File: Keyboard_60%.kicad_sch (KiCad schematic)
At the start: 51 parts, among them J3 Prog_conn, J5 Tag connect TC2030-CTX, SW2 Reset Switch, U3 nRF52840-QIAA-R/nRF52833-QIAA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, Y1 32MHz, Y2 32.768kHz

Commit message: Finalized hardware Ver 1 release
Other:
- company: (none) -> HW-tinkerers
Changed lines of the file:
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@@
   (title_block
     (title "Main Page")
-    (date "2023-06-05")
+    (date "2024-02-17")
     (rev "1.0")
+    (company "HW-tinkerers")
   )
   (junction (at 96.52 181.61) (diameter 0) (color 0 0 0 0)

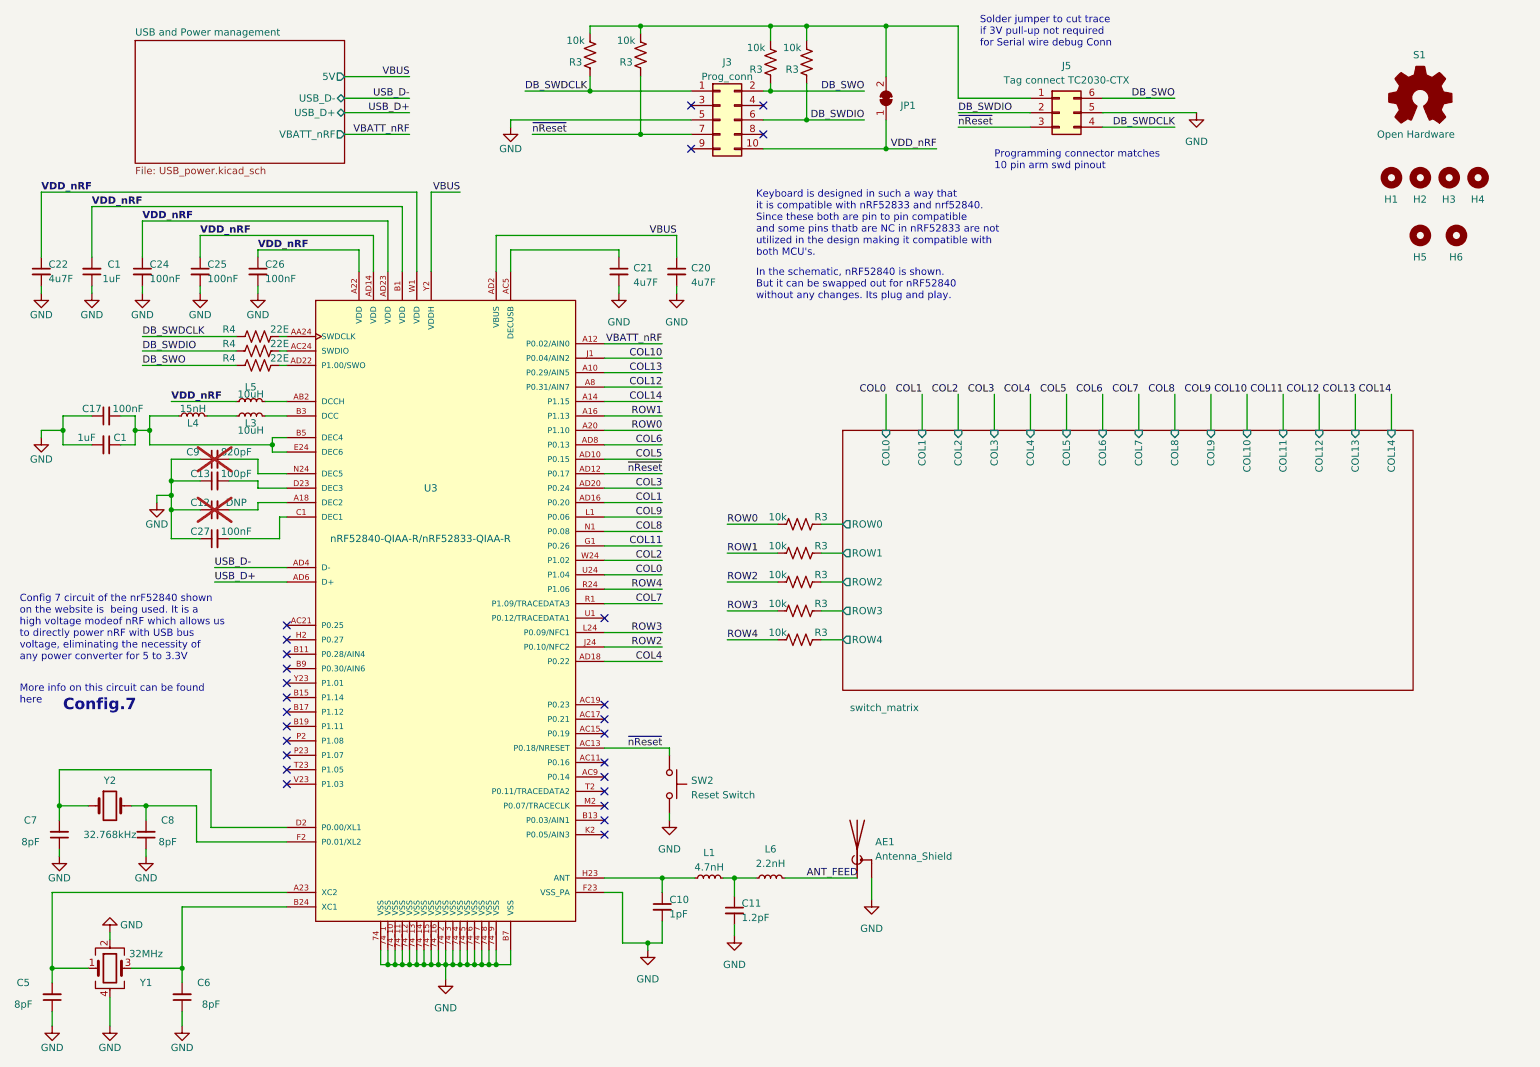
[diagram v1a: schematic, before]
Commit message: Exported edge cuts as footprint and set grid origin
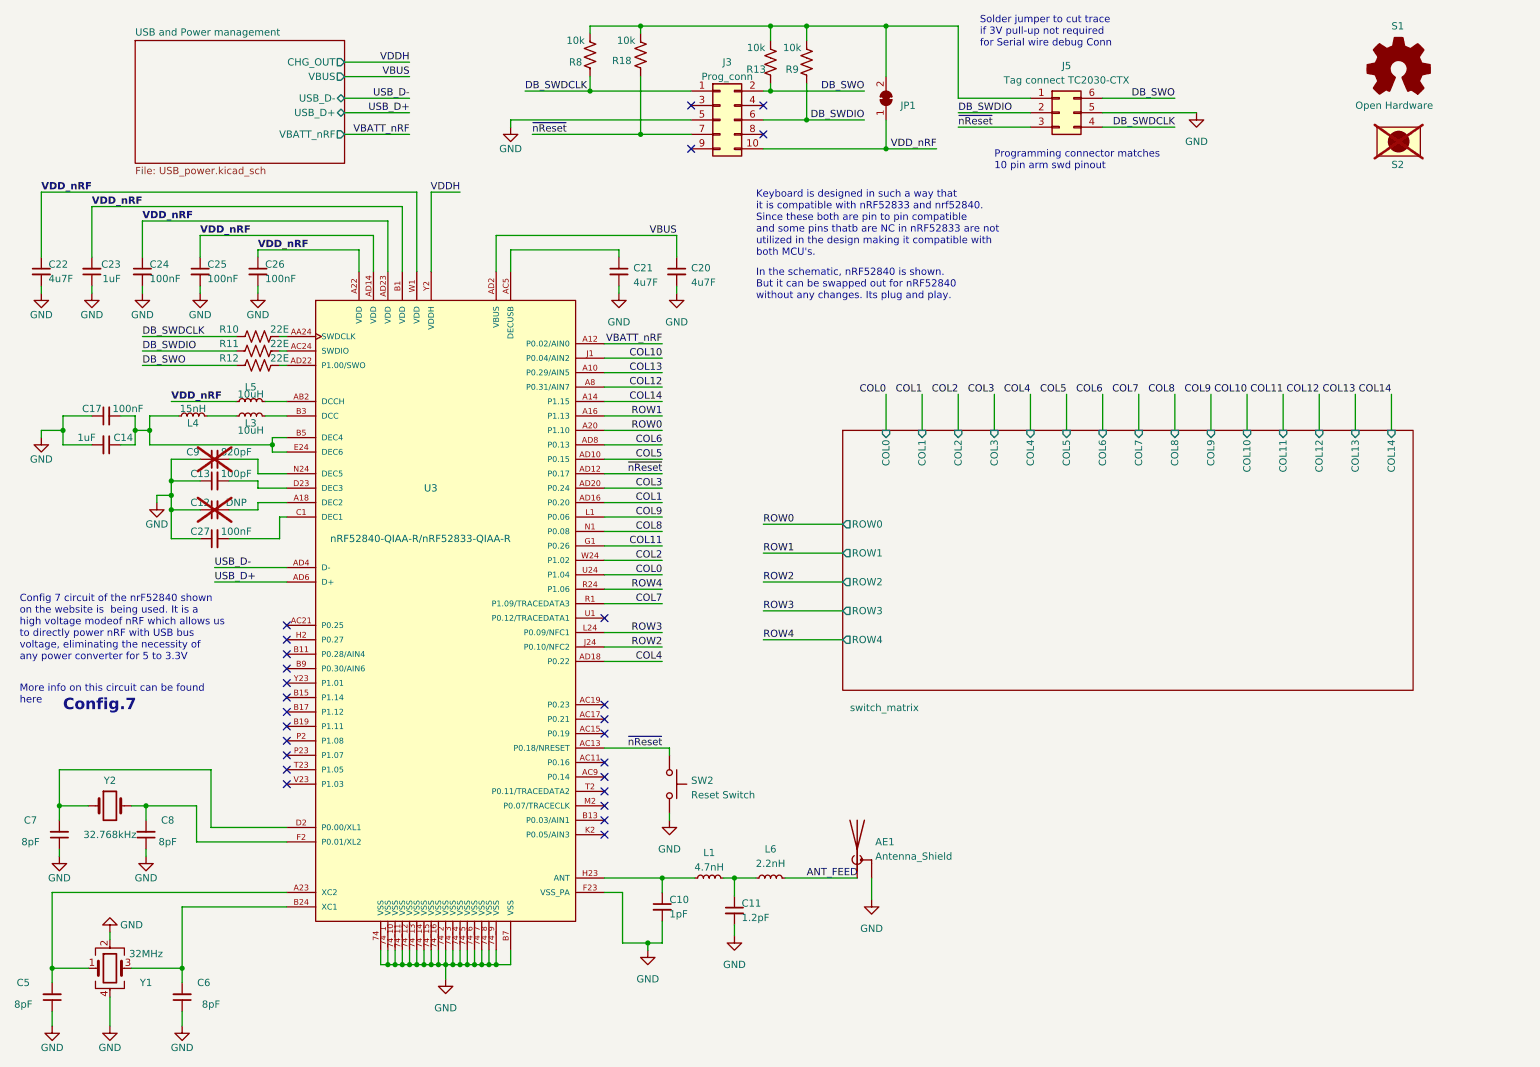
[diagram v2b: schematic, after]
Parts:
- removed H1, H2, H3, H4: MountingHole, keyboard:salvation_mounting_holes, symbol keyboard:MountingHole
- removed H5, H6: MountingHole, keyboard:PKRHSL, symbol keyboard:MountingHole
- removed R3 (x5): 10k, keyboard:R_0402_1005Metric, symbol keyboard:R_US
- added S2: ~, keyboard:Keybaord_outline_edgecuts, symbol keyboard:Outline
- renumbered C1 to C14, C1 to C23, R4 to R10, R4 to R11, R4 to R12, R3 to R13, R3 to R18, R3 to R8, R3 to R9
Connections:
- net VBUS: no longer U3.Y2 (VDDH)
- new net VDDH: U3.Y2 (VDDH)
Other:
- sheet USB and Power management ports: added CHG_OUT, VBUS; removed 5V
- moved on the sheet: S1

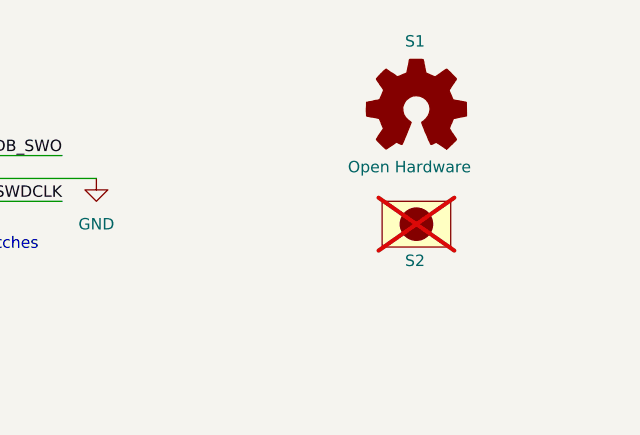
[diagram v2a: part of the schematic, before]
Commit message: Solved all DRC and updated Versioning
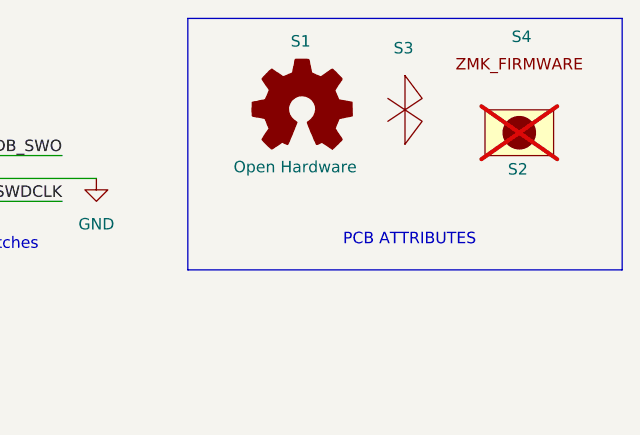
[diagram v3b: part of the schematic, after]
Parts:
- added S3: ~, keyboard:BLE-symbol, symbol keyboard:BLE_SYM
- added S4: ~, keyboard:ZMK_logo, symbol keyboard:ZMK_LOGO
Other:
- note added: "PCB ATTRIBUTES"
- moved on the sheet: S1, S2
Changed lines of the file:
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@@
 		)
 	)
+	(bus
+		(pts
+			(xy 233.68 13.97) (xy 233.68 41.91)
+		)
+		(stroke
+			(width 0)
+			(type default)
+		)
+	)
 	(wire
 		(pts
@@
 		)
 	)
+	(bus
+		(pts
+			(xy 233.68 13.97) (xy 281.94 13.97)
+		)
+		(stroke
+			(width 0)
+			(type default)
+		)
+	)
 	(wire
 		(pts
@@
 		)
 	)
+	(bus
+		(pts
+			(xy 281.94 41.91) (xy 233.68 41.91)
+		)
+		(stroke
+			(width 0)
+			(type default)
+		)
+	)
 	(wire
 		(pts
@@
 		)
 	)
+	(bus
+		(pts
+			(xy 281.94 13.97) (xy 281.94 41.91)
+		)
+		(stroke
+			(width 0)
+			(type default)
+		)
+	)
 	(wire
 		(pts
@@
 		)
 	)
+	(text "PCB ATTRIBUTES"
+		(exclude_from_sim no)
+		(at 258.318 38.608 0)
+		(effects
+			(font
+				(size 1.27 1.27)
+			)
+		)
+	)
 	(text "More info on this circuit can be found\nhere\n"
 		(exclude_from_sim no)
@@
 	(symbol
 		(lib_id "keyboard:Outline")
-		(at 259.08 36.83 0)
+		(at 270.51 26.67 0)
 		(unit 1)
 		(exclude_from_sim yes)
@@
 		(dnp yes)
 		(property "Reference" "S2"
-			(at 257.81 40.894 0)
+			(at 269.24 30.734 0)
 			(effects
 				(font
@@
 		)
 		(property "Value" "~"
-			(at 264.16 38.1 0)
+			(at 275.59 27.94 0)
 			(effects
 				(font
@@
 		)
 		(property "Footprint" "keyboard:Keybaord_outline_edgecuts"
-			(at 259.08 36.83 0)
+			(at 270.51 26.67 0)
 			(effects
 				(font
@@
 		)
 		(property "Datasheet" ""
-			(at 259.08 36.83 0)
+			(at 270.51 26.67 0)
 			(effects
 				(font
@@
 		)
 		(property "Description" "Keyboard outline"
-			(at 259.08 36.83 0)
+			(at 270.51 26.67 0)
 			(effects
 				(font
@@
 	)
 	(symbol
+		(lib_id "keyboard:BLE_SYM")
+		(at 257.81 24.13 0)
+		(unit 1)
+		(exclude_from_sim no)
+		(in_bom yes)
+		(on_board yes)
+		(dnp no)
+		(property "Reference" "S3"
+			(at 256.54 17.272 0)
+			(effects
+				(font
+					(size 1.27 1.27)
+				)
+				(justify left)
+			)
+		)
+		(property "Value" "~"
+			(at 260.35 25.4 0)
+			(effects
+				(font
+					(size 1.27 1.27)
+				)
+				(justify left)
+			)
+		)
+		(property "Footprint" "keyboard:BLE-symbol"
+			(at 257.81 24.13 0)
+			(effects
+				(font
+					(size 1.27 1.27)
+				)
+				(hide yes)
+			)
+		)
+		(property "Datasheet" ""
+			(at 257.81 24.13 0)
+			(effects
+				(font
+					(size 1.27 1.27)
+				)
+				(hide yes)
+			)
+		)
+		(property "Description" ""
+			(at 257.81 24.13 0)
+			(effects
+				(font
+					(size 1.27 1.27)
+				)
+				(hide yes)
+			)
+		)
+		(instances
+			(project "Keyboard_60%"
+				(path "/ef112b03-6536-453f-8127-17d1495b48aa"
+					(reference "S3")
+					(unit 1)
+				)
+			)
+		)
+	)
+	(symbol
 		(lib_id "keyboard:C_Small")
 		(at 50.8 92.71 90)
@@
 	(symbol
 		(lib_id "keyboard:Logo_Open_Hardware_Small")
-		(at 259.08 24.13 0)
+		(at 246.38 24.13 0)
 		(unit 1)
 		(exclude_from_sim no)
 		(in_bom no)
-		(on_board no)
+		(on_board yes)
 		(dnp no)
 		(property "Reference" "S1"
-			(at 257.81 16.51 0)
+			(at 245.11 16.51 0)
 			(effects
 				(font
@@
 		)
 		(property "Value" "Open  Hardware"
-			(at 251.46 30.48 0)
+			(at 238.76 30.48 0)
 			(effects
 				(font
@@
 		)
 		(property "Footprint" "keyboard:OSHW-Logo"
-			(at 259.08 24.13 0)
+			(at 246.38 24.13 0)
 			(effects
 				(font
@@
 		)
 		(property "Datasheet" "~"
-			(at 259.08 24.13 0)
+			(at 246.38 24.13 0)
 			(effects
 				(font
@@
 		)
 		(property "Description" ""
-			(at 259.08 24.13 0)
+			(at 246.38 24.13 0)
 			(effects
 				(font
@@
 					(unit 1)
 				)
+			)
+		)
+	)
+	(symbol
+		(lib_id "keyboard:ZMK_LOGO")
+		(at 270.51 19.05 0)
+		(unit 1)
+		(exclude_from_sim no)
+		(in_bom yes)
+		(on_board yes)
+		(dnp no)
+		(property "Reference" "S4"
+			(at 270.764 16.002 0)
+			(effects
+				(font
+					(size 1.27 1.27)
+				)
+			)
+		)
+		(property "Value" "~"
+			(at 270.51 16.51 0)
+			(effects
+				(font
+					(size 1.27 1.27)
+				)
+			)
+		)
+		(property "Footprint" "keyboard:ZMK_logo"
+			(at 270.51 19.05 0)
+			(effects
+				(font
+					(size 1.27 1.27)
+				)
+				(hide yes)
+			)
+		)
+		(property "Datasheet" ""
+			(at 270.51 19.05 0)
+			(effects
+				(font
+					(size 1.27 1.27)
+				)
+				(hide yes)
+			)
+		)
+		(property "Description" ""
+			(at 270.51 19.05 0)
+			(effects
+				(font
+					(size 1.27 1.27)
+				)
+				(hide yes)
+			)
+		)
+		(instances
+			(project "Keyboard_60%"
+				(path "/ef112b03-6536-453f-8127-17d1495b48aa"
+					(reference "S4")
+					(unit 1)
+				)
